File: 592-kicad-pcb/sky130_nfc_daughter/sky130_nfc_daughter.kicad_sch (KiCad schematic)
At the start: 95 parts, among them J1 U.FL-R-SMT-1_80_, J10 U.FL-R-SMT-1_80_, J2 U.FL-R-SMT-1_80_, J3 U.FL-R-SMT-1_80_, J4 U.FL-R-SMT-1_80_, J5 U.FL-R-SMT-1_80_, J6 U.FL-R-SMT-1_80_, J7 U.FL-R-SMT-1_80_, J8 DF40C-40DS-0.4V_51_, J9 DF40C-40DS-0.4V_51_, SW1 SW_Push, U1 Caravel_QFN, U3 W25Q32JVZP

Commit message: complete signal routing on daughterboard, TODO: power/gnd connections
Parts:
- added C30: 0.1uf, Capacitor_SMD:C_0402_1005Metric, symbol Device:C
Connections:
- net GND: now also J8.39, J9.22, J9.29, C30.2; no longer J9.36, J9.37, J9.39
- net J_ext_clk_dig: now also J9.33; no longer J9.22
- net NFC_AFE_TDO_EXT: now also J9.39; no longer J9.33
- net RESET_EXT: now also J9.38; no longer J9.29
- net VREF_EXT: now also J9.36; no longer J9.38
- net flash_rstb: now also C30.1
- net JB_vdda_user_3v3: now reaches J8.27, JP8.2 (B)
- net J_VDD_EXT: now reaches JP11.1 (A)
- net J_VDD_EXT: now also J9.37; no longer J8.39
- net J_vccd_mgmt_1v8: now reaches J9.2, JP6.1 (A)
- net J_vddio_vdda_mgmt_3v3: now reaches J9.4, JP7.1 (A)
- net J_vccd_user_1v8: now reaches J8.33, JP9.2 (B)
- net JA_vdda_user_3v3: now reaches J8.14, JP10.1 (A)
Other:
- note added: "Debounce"
- moved on the sheet: C11, C12, C13, C22, C23, C27, C4, C5, C6, C7, C8, C9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

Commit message: daughterboard routing, 90% done
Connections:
- net GND: now also J6.3, J8.14; no longer J8.1
- net JA_vdda_user_3v3: now also J8.1; no longer J8.14
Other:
- moved on the sheet: JP10

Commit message: finish daughter routing + silk
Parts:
- C1: renamed from C30; Characteristics 100n 0402 -> (none); LCSC C100072 -> (none); MPN CL05A104KA5NNNC -> (none); MPN_ALT GRM155R71E104KE14J -> (none)
- C10: renamed from C20; Characteristics 1u 0603 -> (none); DigikeyPN 490-12330-1-ND -> (none); Display Value 1u -> (none); LCSC C5673 -> (none); MPN GRT188R61H105KE13D -> (none)
- C11: renamed from C12; Characteristics 100n 0402 -> (none); LCSC C100072 -> (none); MPN CL05A104KA5NNNC -> (none); MPN_ALT GRM155R71E104KE14J -> (none)
- C12: renamed from C13; Characteristics 100n 0402 -> (none); LCSC C100072 -> (none); MPN CL05A104KA5NNNC -> (none); MPN_ALT GRM155R71E104KE14J -> (none)
- C13: renamed from C24; Characteristics 1u 0603 -> (none); DigikeyPN 490-12330-1-ND -> (none); Display Value 1u -> (none); LCSC C5673 -> (none); MPN GRT188R61H105KE13D -> (none)
- C14: renamed from C21; Characteristics 1u 0603 -> (none); DigikeyPN 490-12330-1-ND -> (none); Display Value 1u -> (none); LCSC C5673 -> (none); MPN GRT188R61H105KE13D -> (none)
- C15: renamed from C11; Characteristics 100n 0402 -> (none); LCSC C100072 -> (none); MPN CL05A104KA5NNNC -> (none); MPN_ALT GRM155R71E104KE14J -> (none)
- C16: renamed from C6; Characteristics 100n 0402 -> (none); LCSC C100072 -> (none); MPN CL05A104KA5NNNC -> (none); MPN_ALT GRM155R71E104KE14J -> (none)
- C17: renamed from C8; Characteristics 100n 0402 -> (none); LCSC C100072 -> (none); MPN CL05A104KA5NNNC -> (none); MPN_ALT GRM155R71E104KE14J -> (none)
- C18: renamed from C25; Characteristics 1u 0603 -> (none); DigikeyPN 490-12330-1-ND -> (none); Display Value 1u -> (none); LCSC C5673 -> (none); MPN GRT188R61H105KE13D -> (none)
- C19: renamed from C29; Characteristics 1u 0603 -> (none); DigikeyPN 490-12330-1-ND -> (none); Display Value 1u -> (none); LCSC C5673 -> (none); MPN GRT188R61H105KE13D -> (none)
- C2: renamed from C9; Characteristics 100n 0402 -> (none); LCSC C100072 -> (none); MPN CL05A104KA5NNNC -> (none); MPN_ALT GRM155R71E104KE14J -> (none)
- C20: renamed from C5; Characteristics 100n 0402 -> (none); LCSC C100072 -> (none); MPN CL05A104KA5NNNC -> (none); MPN_ALT GRM155R71E104KE14J -> (none)
- C21: renamed from C14; Characteristics 1u 0603 -> (none); DigikeyPN 490-12330-1-ND -> (none); Display Value 1u -> (none); LCSC C5673 -> (none); MPN GRT188R61H105KE13D -> (none)
- C22: Characteristics 100n 0402 -> (none); LCSC C100072 -> (none); MPN CL05A104KA5NNNC -> (none); MPN_ALT GRM155R71E104KE14J -> (none)
- C23: renamed from C27; Characteristics 100n 0402 -> (none); LCSC C100072 -> (none); MPN CL05A104KA5NNNC -> (none); MPN_ALT GRM155R71E104KE14J -> (none)
- C24: renamed from C18; Characteristics 1u 0603 -> (none); DigikeyPN 490-12330-1-ND -> (none); Display Value 1u -> (none); LCSC C5673 -> (none); MPN GRT188R61H105KE13D -> (none)
- C25: renamed from C23; Characteristics 1u 0603 -> (none); DigikeyPN 490-12330-1-ND -> (none); Display Value 1u -> (none); LCSC C5673 -> (none); MPN GRT188R61H105KE13D -> (none)
- C26: renamed from C15; now fitted
- C27: renamed from C26; now fitted
- C28: renamed from C16; now fitted
- C29: renamed from C28; now fitted
- C3: renamed from C10; Characteristics 1u 0603 -> (none); DigikeyPN 490-12330-1-ND -> (none); Display Value 1u -> (none); LCSC C5673 -> (none); MPN GRT188R61H105KE13D -> (none)
- C30: renamed from C31; now fitted
- C31: renamed from C17; now fitted
- C4: renamed from C2; Characteristics 1u 0603 -> (none); DigikeyPN 490-12330-1-ND -> (none); Display Value 1u -> (none); LCSC C5673 -> (none); MPN GRT188R61H105KE13D -> (none)
- C5: renamed from C19; Characteristics 1u 0603 -> (none); DigikeyPN 490-12330-1-ND -> (none); Display Value 1u -> (none); LCSC C5673 -> (none); MPN GRT188R61H105KE13D -> (none)
- C6: renamed from C3; Characteristics 100n 0402 -> (none); LCSC C100072 -> (none); MPN CL05A104KA5NNNC -> (none); MPN_ALT GRM155R71E104KE14J -> (none)
- C7: renamed from C1; Characteristics 1u 0603 -> (none); DigikeyPN 490-12330-1-ND -> (none); Display Value 1u -> (none); LCSC C5673 -> (none); MPN GRT188R61H105KE13D -> (none)
- C8: renamed from C4; Characteristics 100n 0402 -> (none); LCSC C100072 -> (none); MPN CL05A104KA5NNNC -> (none); MPN_ALT GRM155R71E104KE14J -> (none)
- C9: renamed from C7; Characteristics 100n 0402 -> (none); LCSC C100072 -> (none); MPN CL05A104KA5NNNC -> (none); MPN_ALT GRM155R71E104KE14J -> (none)
- FID1, FID2: now fitted
- J1: renamed from J3; Height 1.45 -> (none); Manufacturer_Name Hirose -> (none); Manufacturer_Part_Number U.FL-R-SMT-1(80) -> (none); Mouser Part Number 798-UFLRSMT180 -> (none); Mouser Price/Stock https://www.mouser.co.uk/ProductDetail/Hirose-Connector/U.F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 -> (none)
- J10: renamed from J8; Height 1.65 -> (none); Manufacturer_Name Hirose -> (none); Manufacturer_Part_Number DF40C-40DS-0.4V(51) -> (none); Mouser Part Number 798-DF40C40DS0.4V51 -> (none); Mouser Price/Stock https://www.mouser.co.uk/ProductDetail/Hirose-Connector/DF4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 -> (none)
- J2: renamed from J4; Height 1.45 -> (none); Manufacturer_Name Hirose -> (none); Manufacturer_Part_Number U.FL-R-SMT-1(80) -> (none); Mouser Part Number 798-UFLRSMT180 -> (none); Mouser Price/Stock https://www.mouser.co.uk/ProductDetail/Hirose-Connector/U.F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 -> (none)
- J3: renamed from J1; Height 1.45 -> (none); Manufacturer_Name Hirose -> (none); Manufacturer_Part_Number U.FL-R-SMT-1(80) -> (none); Mouser Part Number 798-UFLRSMT180 -> (none); Mouser Price/Stock https://www.mouser.co.uk/ProductDetail/Hirose-Connector/U.F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 -> (none)
- J4: renamed from J6; Height 1.45 -> (none); Manufacturer_Name Hirose -> (none); Manufacturer_Part_Number U.FL-R-SMT-1(80) -> (none); Mouser Part Number 798-UFLRSMT180 -> (none); Mouser Price/Stock https://www.mouser.co.uk/ProductDetail/Hirose-Connector/U.F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 -> (none)
- J5: Height 1.45 -> (none); Manufacturer_Name Hirose -> (none); Manufacturer_Part_Number U.FL-R-SMT-1(80) -> (none); Mouser Part Number 798-UFLRSMT180 -> (none); Mouser Price/Stock https://www.mouser.co.uk/ProductDetail/Hirose-Connector/U.F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 -> (none)
- J6: renamed from J7; Height 1.45 -> (none); Manufacturer_Name Hirose -> (none); Manufacturer_Part_Number U.FL-R-SMT-1(80) -> (none); Mouser Part Number 798-UFLRSMT180 -> (none); Mouser Price/Stock https://www.mouser.co.uk/ProductDetail/Hirose-Connector/U.F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 -> (none)
- J7: renamed from J10; Height 1.45 -> (none); Manufacturer_Name Hirose -> (none); Manufacturer_Part_Number U.FL-R-SMT-1(80) -> (none); Mouser Part Number 798-UFLRSMT180 -> (none); Mouser Price/Stock https://www.mouser.co.uk/ProductDetail/Hirose-Connector/U.F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 -> (none)
- J8: renamed from J2; Height 1.45 -> (none); Manufacturer_Name Hirose -> (none); Manufacturer_Part_Number U.FL-R-SMT-1(80) -> (none); Mouser Part Number 798-UFLRSMT180 -> (none); Mouser Price/Stock https://www.mouser.co.uk/ProductDetail/Hirose-Connector/U.F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 -> (none)
- J9: Height 1.65 -> (none); Manufacturer_Name Hirose -> (none); Manufacturer_Part_Number DF40C-40DS-0.4V(51) -> (none); Mouser Part Number 798-DF40C40DS0.4V51 -> (none); Mouser Price/Stock https://www.mouser.co.uk/ProductDetail/Hirose-Connector/DF4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 -> (none)
- L1: renamed from L4; now fitted
- L2: renamed from L3; now fitted
- R1: renamed from R9; Characteristics 0R 1206 -> (none)
- R11: renamed from R12; now fitted
- R12: renamed from R11; now fitted
- R2: renamed from R8; Characteristics 0R 1206 -> (none)
- R3: renamed from R1; Characteristics 0R 1206 -> (none)
- R4: renamed from R10; Characteristics 0R 1206 -> (none)
- R5: renamed from R7; Characteristics 0R 1206 -> (none)
- R6: Characteristics 0R 1206 -> (none)
- renumbered D16 to D1, D12 to D10, D9 to D11, D8 to D12, D3 to D13, D10 to D14, D2 to D15, D1 to D16, D4 to D2, D15 to D3, D6 to D4, D14 to D5, D7 to D6, D11 to D7, D5 to D8, D13 to D9, JP3 to JP1, JP12 to JP10, JP5 to JP11, JP2 to JP12, JP6 to JP2, JP7 to JP3, JP10 to JP4, JP8 to JP5, JP9 to JP6, JP11 to JP7, JP1 to JP8, JP4 to JP9, R5 to R10, R4 to R7, R3 to R8, R2 to R9, TP4 to TP1, TP1 to TP4, U3 to U1, U1 to U2

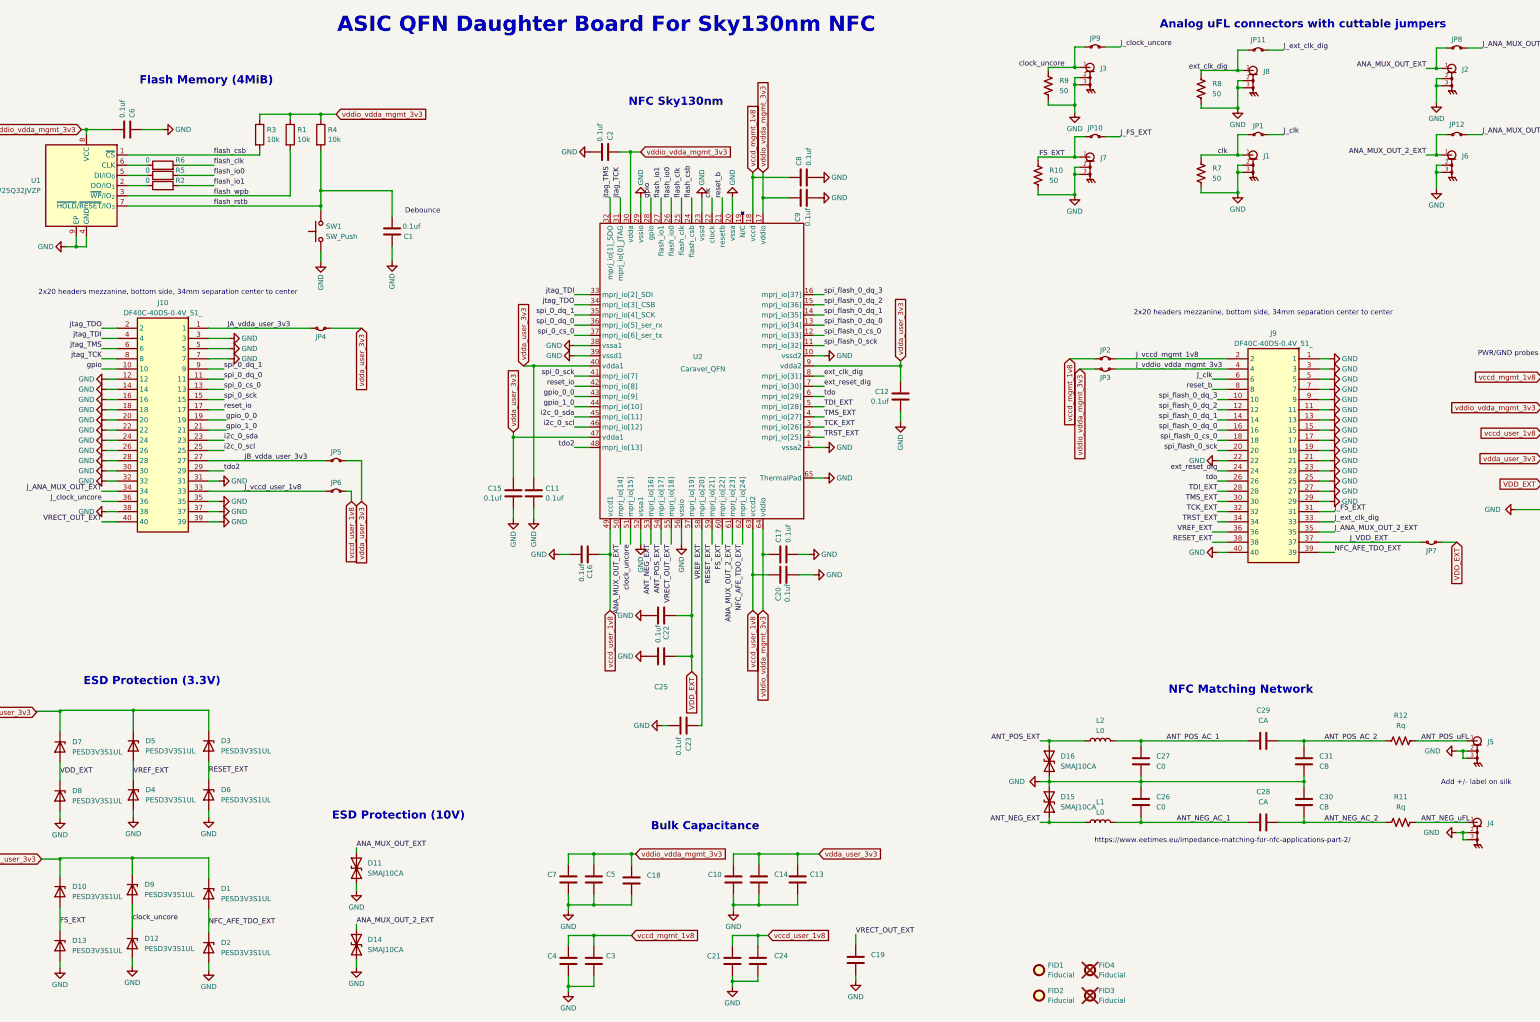
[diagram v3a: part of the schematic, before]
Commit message: add qfn small epad footprint, update silk on daughterboard, add fiducials, adjust mezzanine spacing
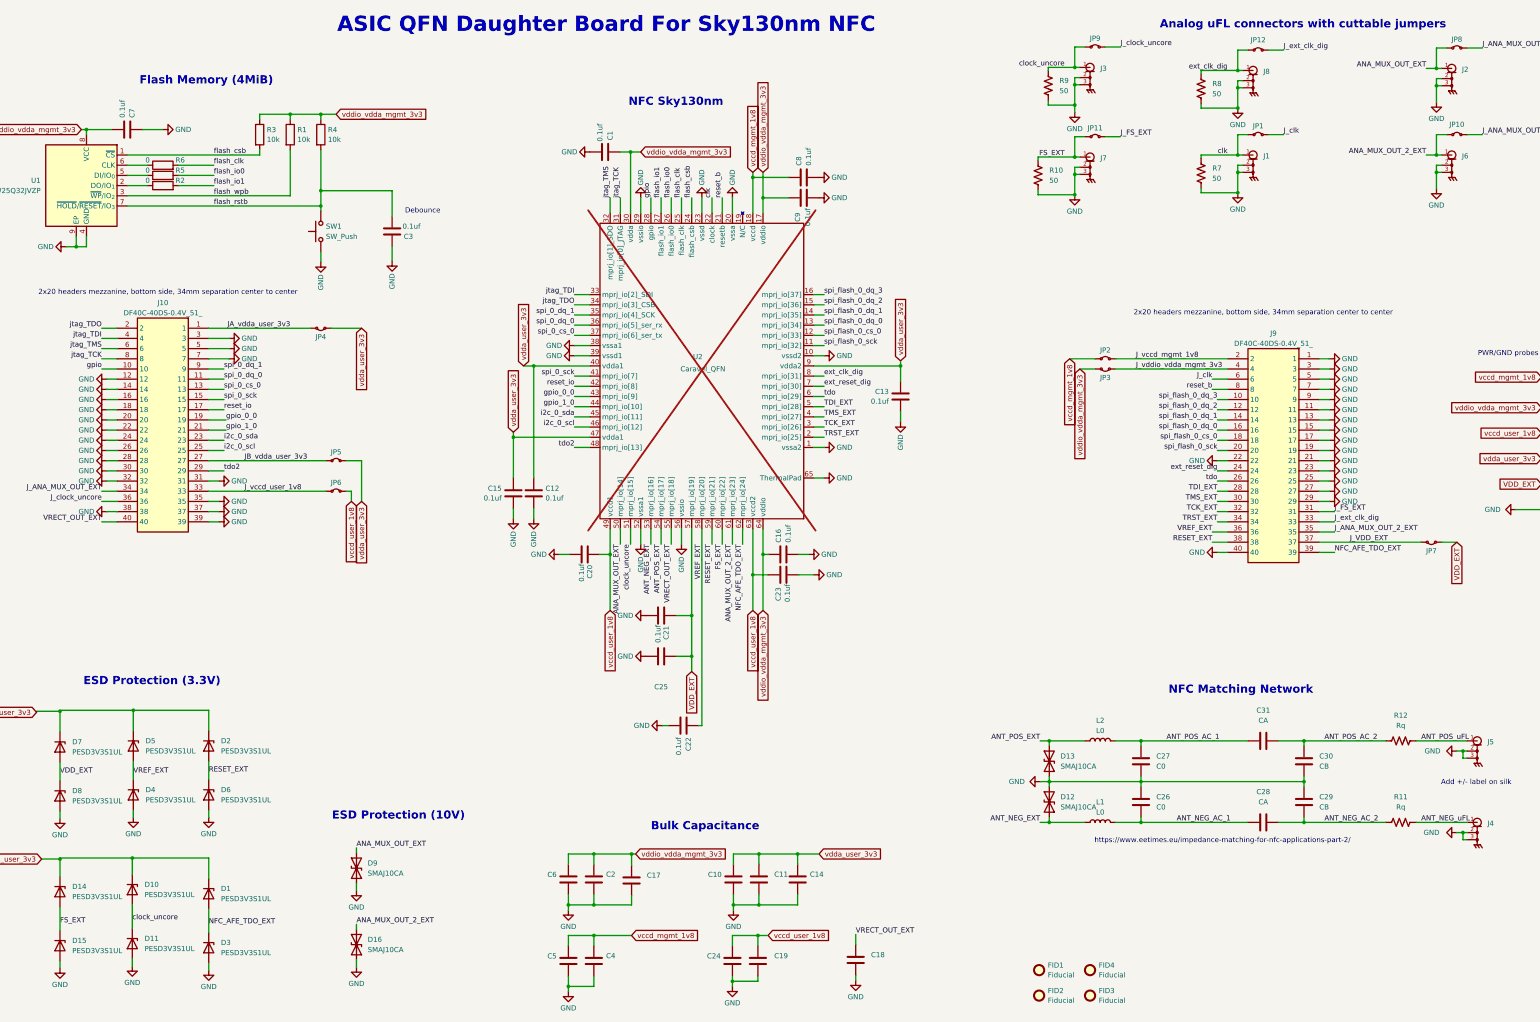
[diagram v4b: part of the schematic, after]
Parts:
- FID3, FID4: now fitted
- U2: footprint Package_DFN_QFN:QFN-64-1EP_9x9mm_P0.5mm_EP7.65x7.65mm -> 592-partslib:QFN-64-1EP_9x9mm_P0.5mm_EP7.65x7.65mm_SMALL_EPAD; now not fitted
- renumbered C2 to C1, C14 to C11, C11 to C12, C12 to C13, C13 to C14, C17 to C16, C18 to C17, C19 to C18, C24 to C19, C5 to C2, C16 to C20, C22 to C21, C23 to C22, C20 to C23, C21 to C24, C30 to C29, C1 to C3, C31 to C30, C29 to C31, C3 to C4, C4 to C5, C7 to C6, C6 to C7, D9 to D10, D12 to D11, D15 to D12, D16 to D13, D10 to D14, D13 to D15, D14 to D16, D3 to D2, D2 to D3, D11 to D9, JP12 to JP10, JP10 to JP11, JP11 to JP12
